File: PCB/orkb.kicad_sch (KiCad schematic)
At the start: 114 parts, among them J1 USB_C_Receptacle_USB2.0, P1 OLED, SW1 MXHS, SW10 MXHS, SW11 MXHS, SW12 MXHS, SW13 MXHS, SW14 MXHS, SW15 MXHS, SW16 MXHS, SW17 MXHS, SW18 MXHS, SW19 MXHS, SW2 MXHS, SW20 MXHS, SW21 MXHS, SW22 MXHS, SW23 MXHS, SW24 MSK12C02, SW25 MSK12C02, SW3 MXHS, SW4 MXHS, SW5 MXHS, SW6 MXHS, SW7 MXHS, SW8 MXHS, SW9 MXHS, U1 ProMicro, U2 SRV05-4, U3 SRV05-4

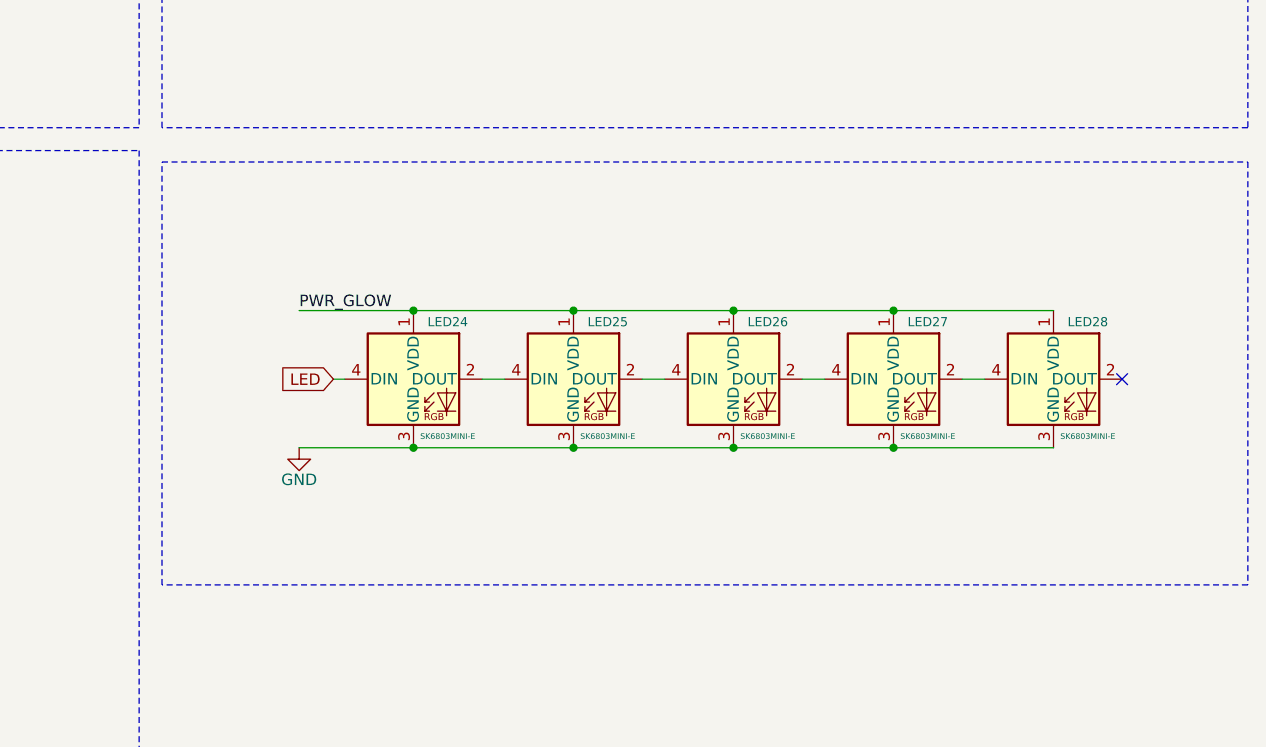
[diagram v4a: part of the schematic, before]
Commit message: Removing under-glow LEDs (for now)
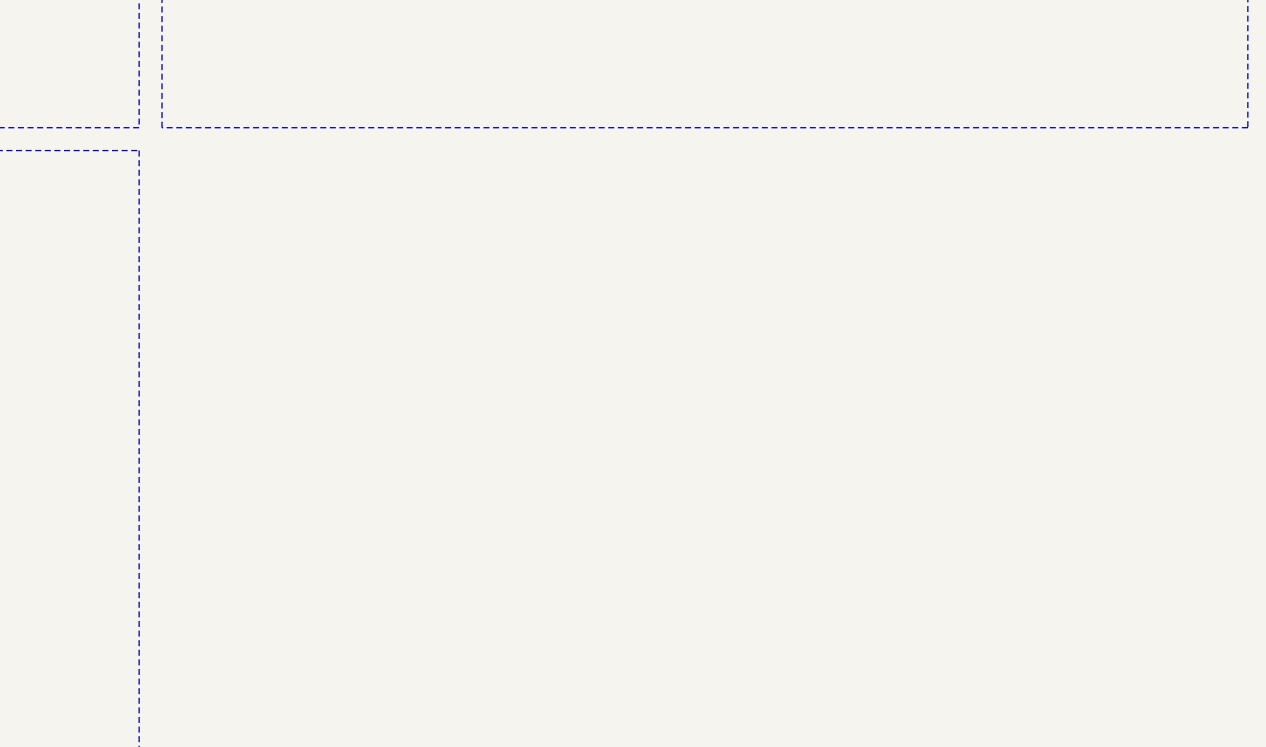
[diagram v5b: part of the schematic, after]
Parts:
- removed LED24, LED25, LED26, LED27, LED28: SK6803MINI-E, SplitKeyboard_Common:MX_SK6812MINI-E_REVERSIBLE, symbol SplitKeyboard_Common:SK6812MINI-E
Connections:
- no-connect marks 14 -> 13

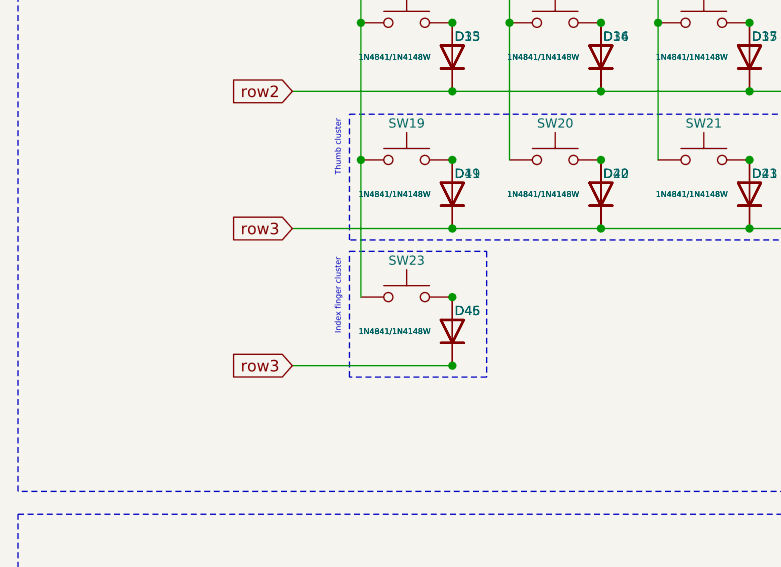
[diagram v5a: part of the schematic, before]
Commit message: Per key RBG, Switch column and row routing complete
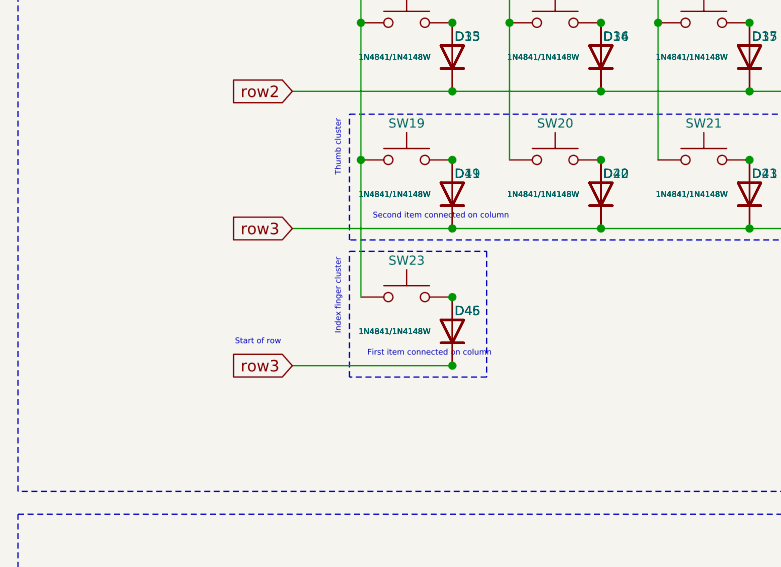
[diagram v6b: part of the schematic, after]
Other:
- note added: "First item connected on column"
- note added: "Second item connected on column"
- note added: "Start of row"
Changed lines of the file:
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@@
+		)
+	)
+	(text "First item connected on column"
+		(exclude_from_sim no)
+		(at 59.69 180.34 0)
+		(effects
+			(font
+				(size 0.635 0.635)
+			)
 		)
 	)
@@
 		)
 	)
+	(text "Second item connected on column"
+		(exclude_from_sim no)
+		(at 60.96 165.1 0)
+		(effects
+			(font
+				(size 0.635 0.635)
+			)
+		)
+	)
 	(text "Thumb cluster"
 		(exclude_from_sim no)
@@
 		(effects
 			(font
+				(size 0.635 0.635)
+			)
+		)
+	)
+	(text "Start of row"
+		(exclude_from_sim no)
+		(at 40.64 179.07 0)
+		(effects
+			(font
